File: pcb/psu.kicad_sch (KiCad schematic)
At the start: 36 parts, among them J201 USB_B_Mini, U201 TPS54325PWPR, U202 TPS54294PWP

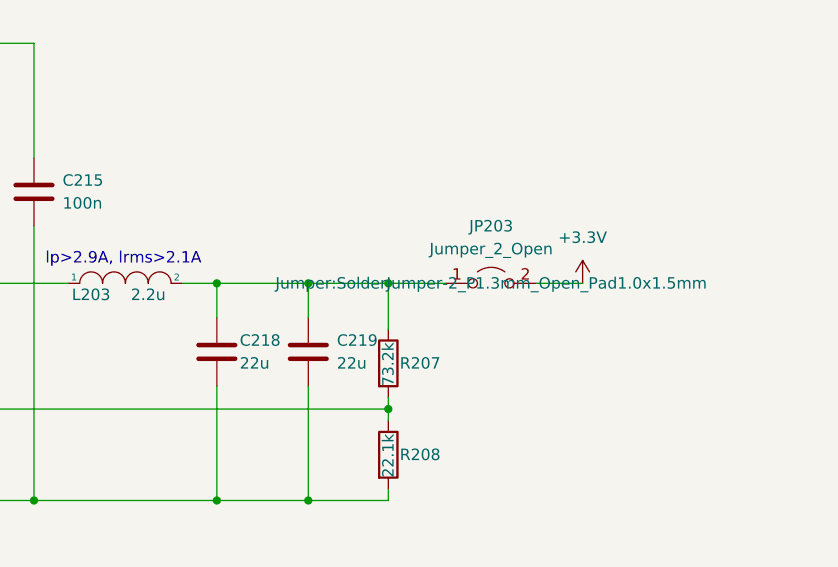
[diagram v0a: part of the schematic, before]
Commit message: replace jumpers with pin headers
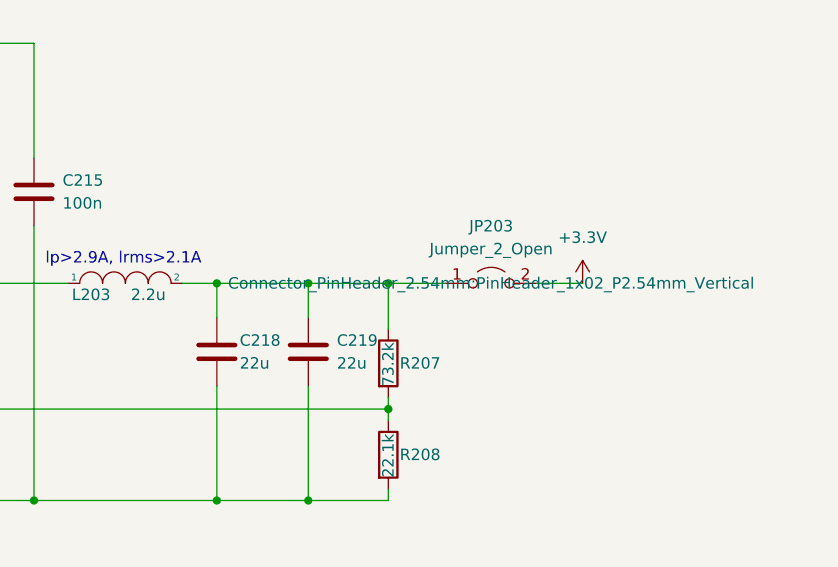
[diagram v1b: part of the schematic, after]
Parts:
- JP201, JP202, JP203: footprint Jumper:SolderJumper-2_P1.3mm_Open_Pad1.0x1.5mm -> Connector_PinHeader_2.54mm:PinHeader_1x02_P2.54mm_Vertical
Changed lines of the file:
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@@
     (property "Reference" "JP201" (id 0) (at 26.67 128.27 0))
     (property "Value" "Jumper_2_Open" (id 1) (at 26.67 130.81 0))
-    (property "Footprint" "Jumper:SolderJumper-2_P1.3mm_Open_Pad1.0x1.5mm" (id 2) (at 26.67 134.62 0)
+    (property "Footprint" "Connector_PinHeader_2.54mm:PinHeader_1x02_P2.54mm_Vertical" (id 2) (at 26.67 134.62 0)
       (effects (font (size 1.27 1.27)) hide)
     )
@@
     (property "Reference" "JP202" (id 0) (at 243.84 43.18 0))
     (property "Value" "Jumper_2_Open" (id 1) (at 243.84 45.72 0))
-    (property "Footprint" "Jumper:SolderJumper-2_P1.3mm_Open_Pad1.0x1.5mm" (id 2) (at 243.84 49.53 0)
+    (property "Footprint" "Connector_PinHeader_2.54mm:PinHeader_1x02_P2.54mm_Vertical" (id 2) (at 243.84 49.53 0)
       (effects (font (size 1.27 1.27)) hide)
     )
@@
     (property "Reference" "JP203" (id 0) (at 265.43 128.27 0))
     (property "Value" "Jumper_2_Open" (id 1) (at 265.43 130.81 0))
-    (property "Footprint" "Jumper:SolderJumper-2_P1.3mm_Open_Pad1.0x1.5mm" (id 2) (at 265.43 134.62 0))
+    (property "Footprint" "Connector_PinHeader_2.54mm:PinHeader_1x02_P2.54mm_Vertical" (id 2) (at 265.43 134.62 0))
     (property "Datasheet" "~" (id 3) (at 265.43 134.62 0)
       (effects (font (size 1.27 1.27)) hide)

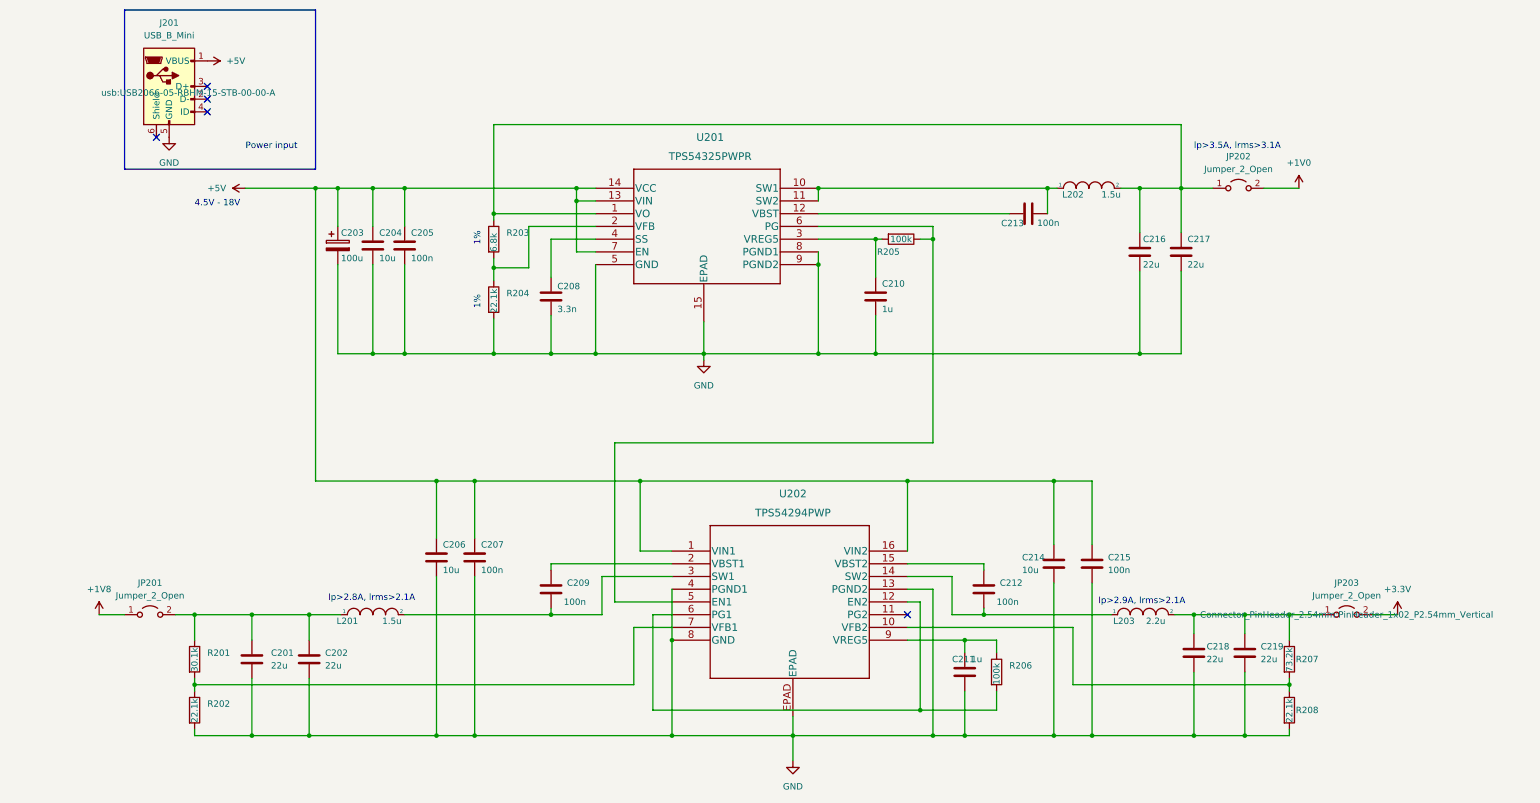
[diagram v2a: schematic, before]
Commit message: fix errors in schematic
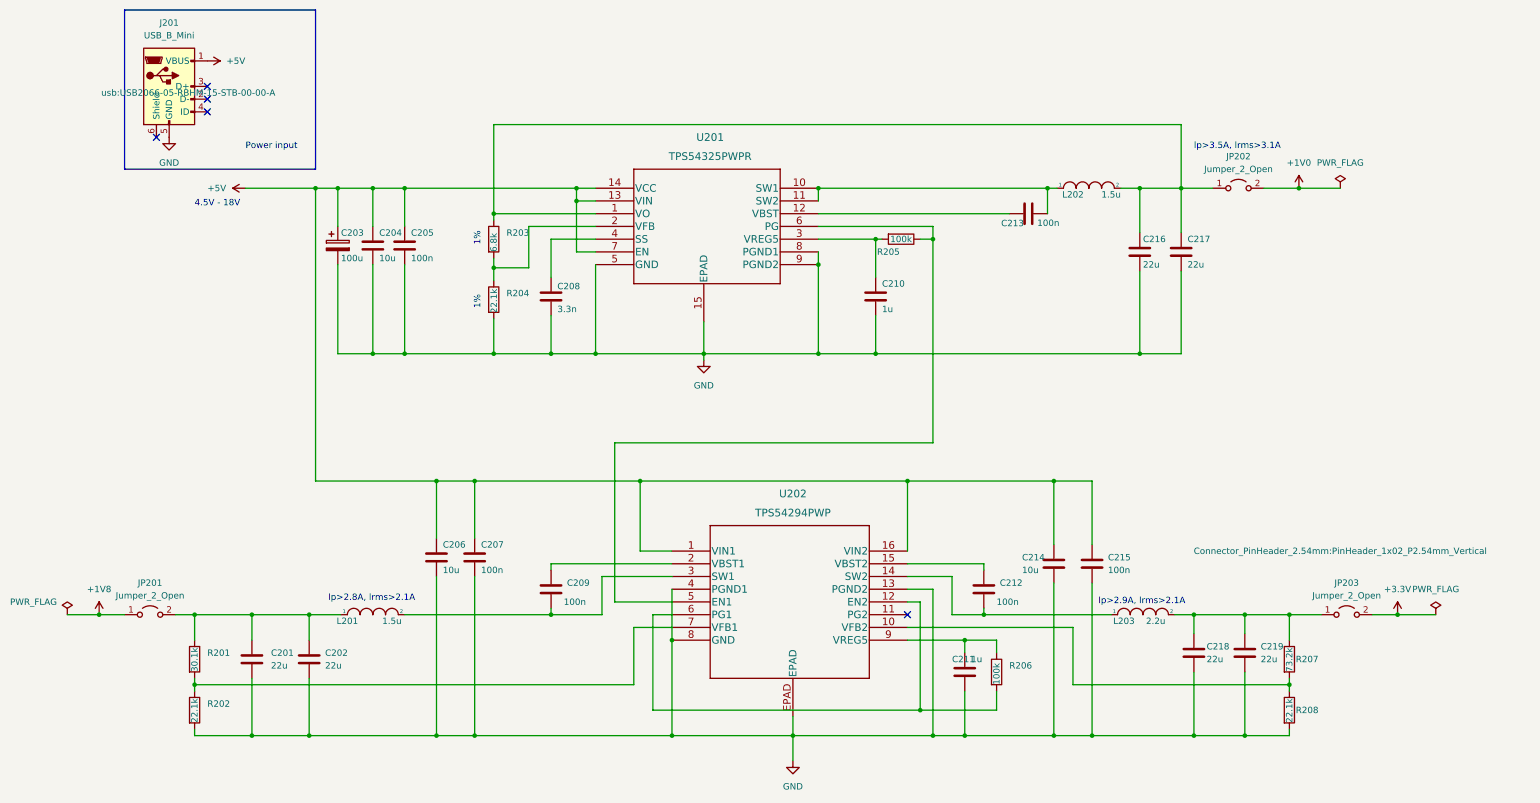
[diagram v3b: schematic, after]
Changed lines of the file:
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@@
   (junction (at 46.99 134.62) (diameter 0) (color 0 0 0 0)
   )
+  (junction (at 255.905 49.53) (diameter 0) (color 0 0 0 0)
+  )
   (junction (at 177.8 107.95) (diameter 0) (color 0 0 0 0)
   )
@@
   (junction (at 224.155 49.53) (diameter 0) (color 0 0 0 0)
   )
+  (junction (at 275.59 134.62) (diameter 0) (color 0 0 0 0)
+  )
   (junction (at 182.88 59.69) (diameter 0) (color 0 0 0 0)
   )
@@
   )
   (junction (at 182.88 158.75) (diameter 0) (color 0 0 0 0)
+  )
+  (junction (at 16.51 134.62) (diameter 0) (color 0 0 0 0)
   )
   (junction (at 71.12 49.53) (diameter 0) (color 0 0 0 0)
@@
     (stroke (width 0) (type default) (color 0 0 0 0))
   )
+  (wire (pts (xy 16.51 134.62) (xy 10.16 134.62))
+    (stroke (width 0) (type default) (color 0 0 0 0))
+  )
   (wire (pts (xy 232.41 49.53) (xy 232.41 58.42))
     (stroke (width 0) (type default) (color 0 0 0 0))
@@
     (stroke (width 0) (type default) (color 0 0 0 0))
   )
+  (wire (pts (xy 275.59 134.62) (xy 283.21 134.62))
+    (stroke (width 0) (type default) (color 0 0 0 0))
+  )
   (wire (pts (xy 254 158.75) (xy 254 157.48))
     (stroke (width 0) (type default) (color 0 0 0 0))
@@
   )
   (polyline (pts (xy 59.69 45.72) (xy 21.59 45.72))
+    (stroke (width 0) (type default) (color 0 0 0 0))
+  )
+  (wire (pts (xy 255.905 49.53) (xy 264.16 49.53))
     (stroke (width 0) (type default) (color 0 0 0 0))
   )
@@
     (pin "6")
   )
+  (symbol (lib_id "power:PWR_FLAG") (at 264.16 49.53 0) (unit 1)
+    (in_bom yes) (on_board yes) (fields_autoplaced)
+    (property "Reference" "#FLG0102" (id 0) (at 264.16 47.625 0)
+      (effects (font (size 1.27 1.27)) hide)
+    )
+    (property "Value" "PWR_FLAG" (id 1) (at 264.16 44.45 0))
+    (property "Footprint" "" (id 2) (at 264.16 49.53 0)
+      (effects (font (size 1.27 1.27)) hide)
+    )
+    (property "Datasheet" "~" (id 3) (at 264.16 49.53 0)
+      (effects (font (size 1.27 1.27)) hide)
+    )
+    (pin "1")
+  )
   (symbol (lib_id "Device:R") (at 95.25 59.69 0) (unit 1)
     (in_bom yes) (on_board yes)
@@
   )
   (symbol (lib_id "Jumper:Jumper_2_Open") (at 265.43 134.62 0) (unit 1)
-    (in_bom yes) (on_board yes) (fields_autoplaced)
+    (in_bom yes) (on_board yes)
     (property "Reference" "JP203" (id 0) (at 265.43 128.27 0))
     (property "Value" "Jumper_2_Open" (id 1) (at 265.43 130.81 0))
-    (property "Footprint" "Connector_PinHeader_2.54mm:PinHeader_1x02_P2.54mm_Vertical" (id 2) (at 265.43 134.62 0))
+    (property "Footprint" "Connector_PinHeader_2.54mm:PinHeader_1x02_P2.54mm_Vertical" (id 2) (at 264.16 121.92 0))
     (property "Datasheet" "~" (id 3) (at 265.43 134.62 0)
       (effects (font (size 1.27 1.27)) hide)
@@
     (pin "2")
   )
+  (symbol (lib_id "power:PWR_FLAG") (at 10.16 134.62 0) (unit 1)
+    (in_bom yes) (on_board yes)
+    (property "Reference" "#FLG0101" (id 0) (at 10.16 132.715 0)
+      (effects (font (size 1.27 1.27)) hide)
+    )
+    (property "Value" "PWR_FLAG" (id 1) (at -1.27 132.08 0)
+      (effects (font (size 1.27 1.27)) (justify left))
+    )
+    (property "Footprint" "" (id 2) (at 10.16 134.62 0)
+      (effects (font (size 1.27 1.27)) hide)
+    )
+    (property "Datasheet" "~" (id 3) (at 10.16 134.62 0)
+      (effects (font (size 1.27 1.27)) hide)
+    )
+    (pin "1")
+  )
   (symbol (lib_id "pspice:INDUCTOR") (at 71.12 134.62 0) (unit 1)
     (in_bom yes) (on_board yes)
@@
     (pin "2")
   )
+  (symbol (lib_id "power:PWR_FLAG") (at 283.21 134.62 0) (unit 1)
+    (in_bom yes) (on_board yes) (fields_autoplaced)
+    (property "Reference" "#FLG0103" (id 0) (at 283.21 132.715 0)
+      (effects (font (size 1.27 1.27)) hide)
+    )
+    (property "Value" "PWR_FLAG" (id 1) (at 283.21 129.54 0))
+    (property "Footprint" "" (id 2) (at 283.21 134.62 0)
+      (effects (font (size 1.27 1.27)) hide)
+    )
+    (property "Datasheet" "~" (id 3) (at 283.21 134.62 0)
+      (effects (font (size 1.27 1.27)) hide)
+    )
+    (pin "1")
+  )
   (symbol (lib_id "power:+5V") (at 45.72 49.53 90) (unit 1)
